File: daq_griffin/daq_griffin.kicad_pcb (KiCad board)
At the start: 4 copper layers, 120 x 120 mm, 223 parts, among them J1 SENSOR, J10 SENSOR, J11 SENSOR, J12 SENSOR, J13 SENSOR, J14 SENSOR, J15 SENSOR, J16 SENSOR, J17 SENSOR, J18 SENSOR, J19 SENSOR, J2 SENSOR, J20 SENSOR, J21 SENSOR, J22 SENSOR, J23 SENSOR, J24 SENSOR, J25 POWER_12V, J26 I2C Header, J27 CAN Header, J28 POWER_24V, J29 POWER_24V, J3 SENSOR, J30 POWER_24V, J31 POWER_24V, J32 POWER_24V, J33 POWER_24V, J34 POWER_24V, J35 POWER_24V, J36 POWER_24V, J37 Conn_01x04_Socket, J38 Conn_01x04_Socket, J39 Conn_01x04_Socket, J4 SENSOR, J40 Conn_01x04_Socket, J41 Conn_01x04_Socket, J42 Conn_01x04_Socket, J43 UART Header, J44 UART Header, J45 Conn_01x03_Socket, J46 Conn_01x03_Socket, J5 SENSOR, J6 SENSOR, J7 SENSOR, J8 SENSOR, J9 SENSOR, U13 ADS8866, U14 ADS8866, U15 ADS8866, U16 ADS8866, U17 ADS8866, U18 ADS8866, U19 ADS8866, U20 ADS8866, U21 ADS8866, U22 ADS8866, U23 ADS8866, U24 ADS8866, U25 TPS54302, U26 Teensy4.1, U29 REF6050xDGK, U30 TLV70933, U55 TCAN3414

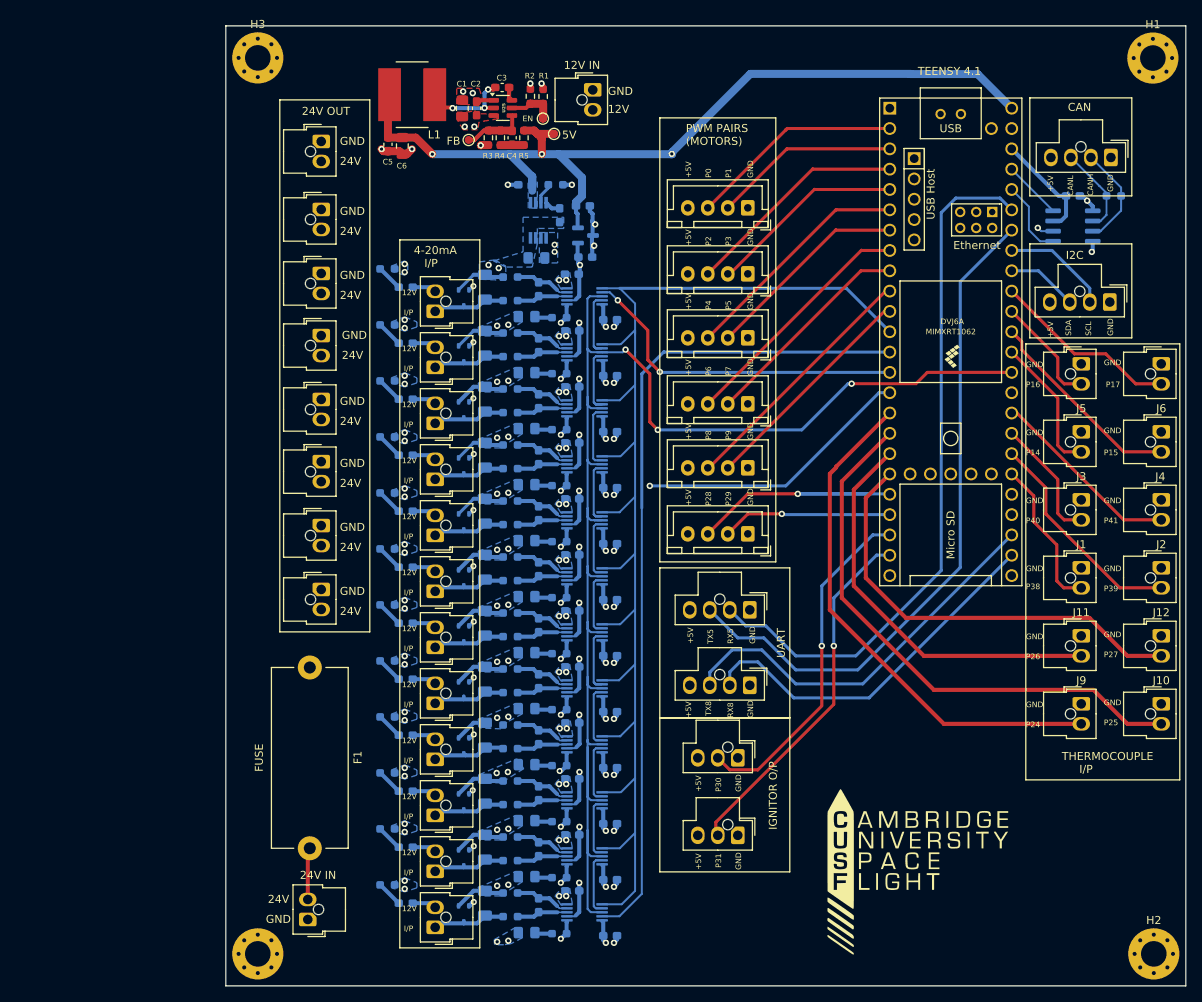
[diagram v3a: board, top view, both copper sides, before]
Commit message: Final touches to silkscreen and hole clearance, names added
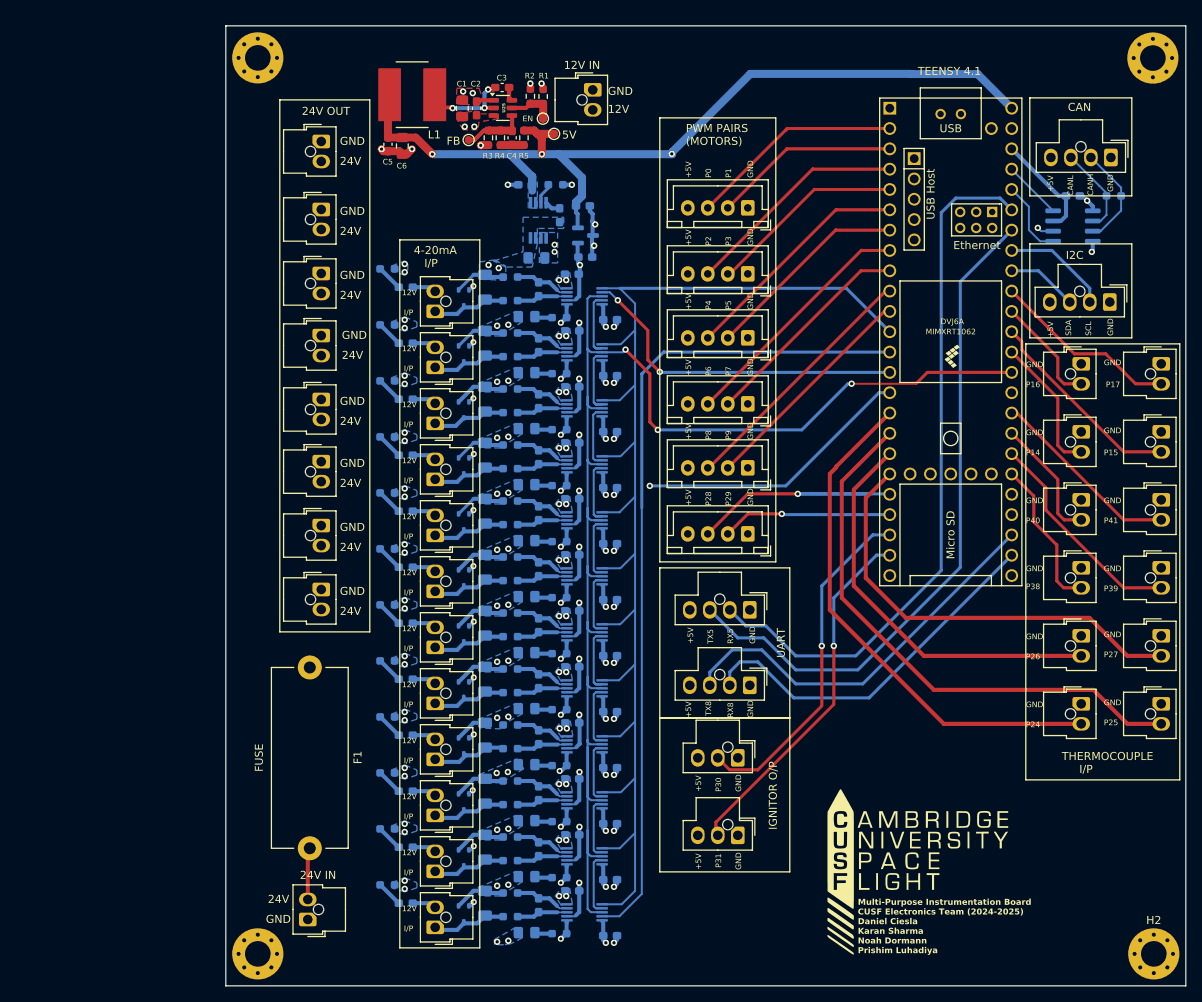
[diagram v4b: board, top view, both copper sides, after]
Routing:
- net /ADC_Chain2/ADC9/SENSOR.IN: track 8.93 -> 9.61 mm
- net /ADC_Chain2/ADC7/SENSOR.IN: track 8.93 -> 9.61 mm
- net /ADC_Chain2/ADC5/SENSOR.IN: track 9.00 -> 9.68 mm
- net /ADC_Chain2/ADC3/SENSOR.IN: track 8.93 -> 9.61 mm
- net /ADC_Chain2/ADC2/SENSOR.IN: track 8.93 -> 9.61 mm
- net /ADC_Chain2/ADC8/SENSOR.IN: track 8.93 -> 9.61 mm
- net /ADC_Chain2/ADC6/SENSOR.IN: track 8.93 -> 9.61 mm
- net /ADC_Chain2/ADC4/SENSOR.IN: track 9.08 -> 9.76 mm
- net /ADC_Chain2/ADC12/SENSOR.IN: track 8.93 -> 9.61 mm
- net /ADC_Chain2/ADC11/SENSOR.IN: track 8.93 -> 9.61 mm
- net /ADC_Chain2/ADC10/SENSOR.IN: track 8.75 -> 9.43 mm
- net /ADC_Chain2/ADC1/SENSOR.IN: track 8.93 -> 9.61 mm
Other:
- board text added: "Multi-Purpose Instrumentation Board CUSF Electronics Team (2024-2025) Daniel Ciesla Karan Sharma Noah Dormann Prishim Luhadiya"

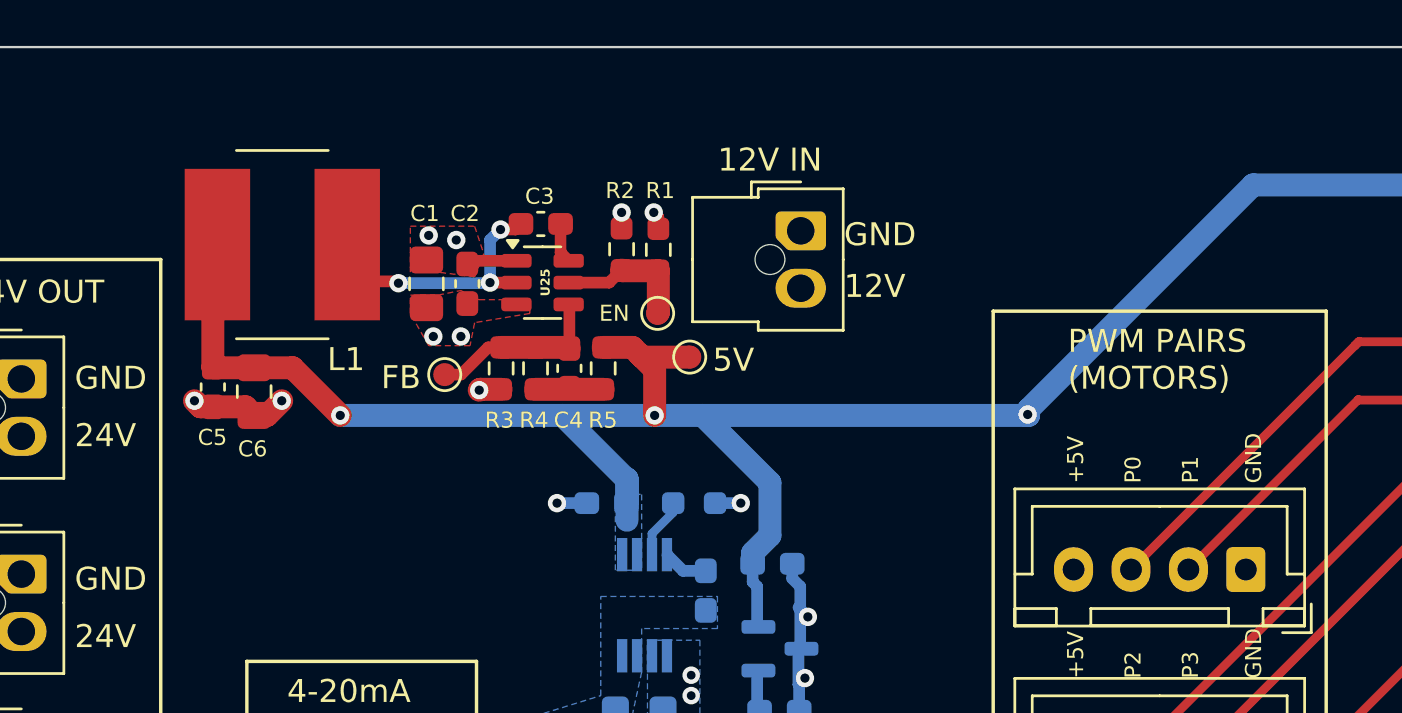
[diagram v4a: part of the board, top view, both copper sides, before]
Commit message: Move 12V - 5V converter circuit to back of board.
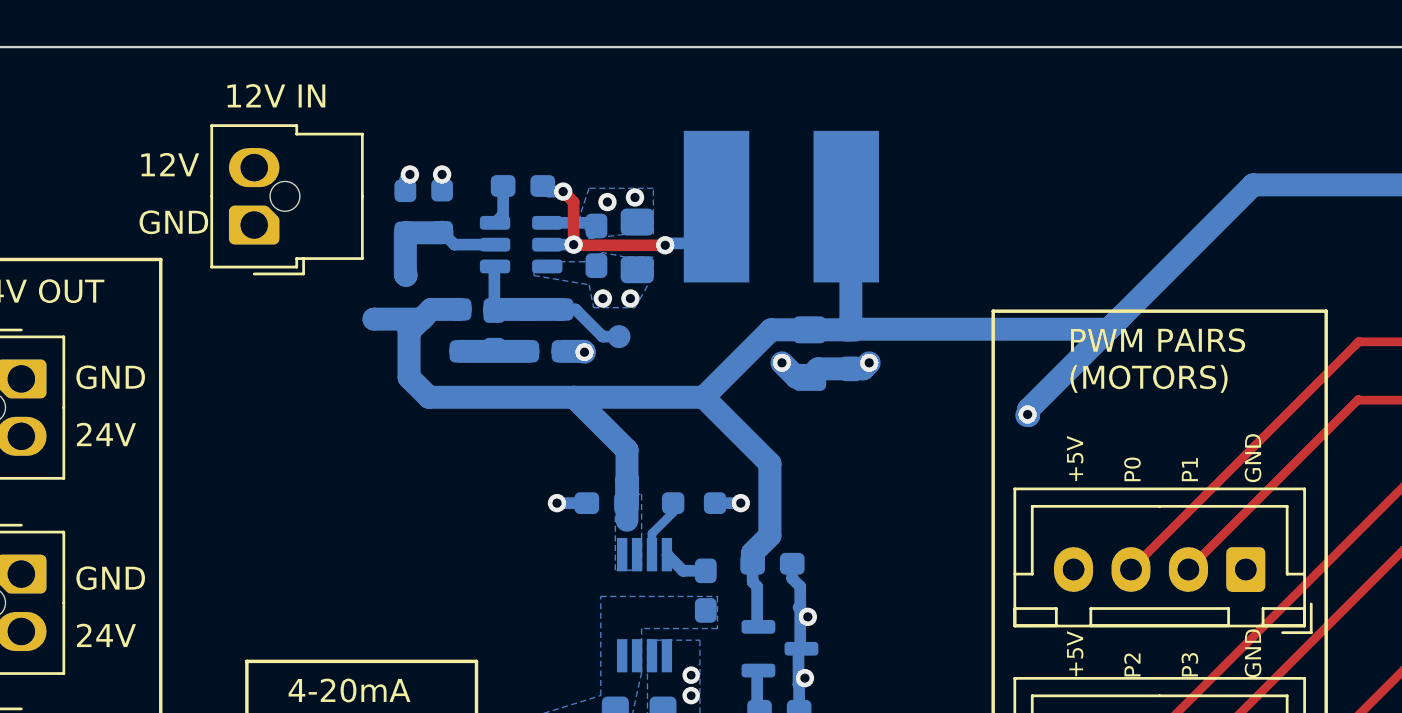
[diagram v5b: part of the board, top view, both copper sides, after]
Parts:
- C1, C2, C3, C4, C5, C6, L1, R1, R2, R3, R4, R5, TP1, TP2, TP3, U25: moved to B.Cu
- moved C5 27.8 mm to (128.1, 71.1)
- moved C6 24.2 mm to (126.3, 71.3)
- moved J25 23.8 mm to (102.1, 65.8), turned to 180 degrees
- moved L1 21.8 mm to (125.0, 64.9), turned to 0 degrees
- moved TP3 13.8 mm to (107.3, 69.8), turned to 180 degrees
- moved R1 11.1 mm to (108.7, 65.2)
- moved TP1 11.1 mm to (108.7, 67.9), turned to 180 degrees
- moved C1 9.33 mm to (118.7, 66.7)
- moved R2 7.99 mm to (110.3, 65.1)
- moved TP2 7.77 mm to (118.0, 70.6), turned to 180 degrees
- moved R5 6.43 mm to (111.1, 70.3)
- moved C2 5.86 mm to (117.0, 66.7)
- moved C4 3.66 mm to (112.5, 70.3)
- moved R3 3.15 mm to (115.5, 70.3)
- moved U25 1.90 mm to (113.7, 66.6), turned to 180 degrees
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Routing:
- net +5V: track 114.7 -> 112.5 mm, vias 3 -> 1
- removed copper zone on F.Cu, net +12V
- removed copper zone on F.Cu, net GND

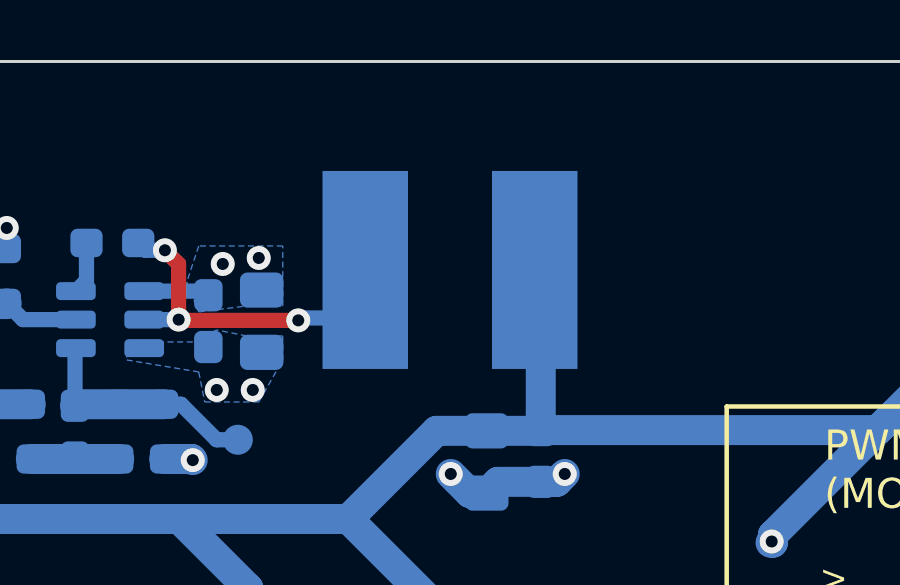
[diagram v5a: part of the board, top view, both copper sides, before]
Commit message: Inductor footprint changed, ADC fuse value now 30mA, ADC 25R resistor now 22R, 0.1-0.47R resistor set to 0.47R
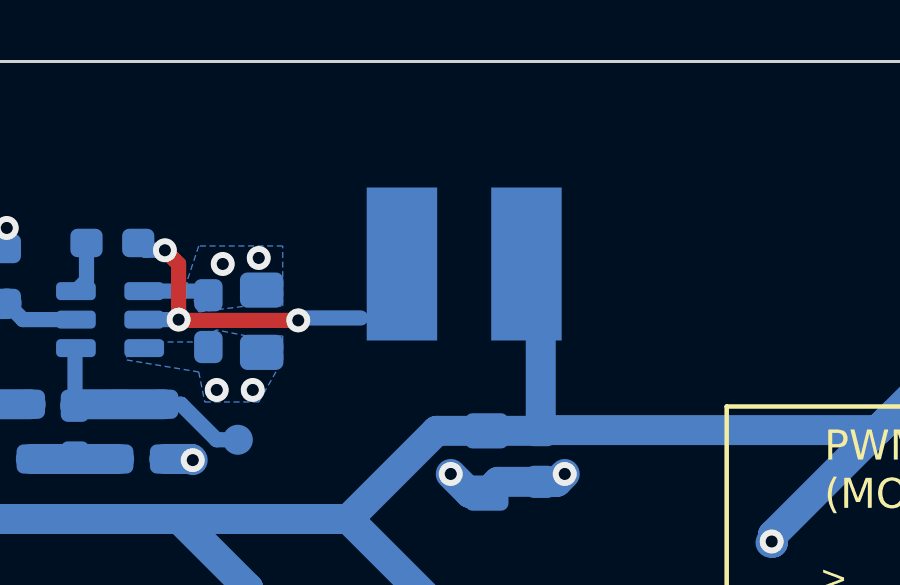
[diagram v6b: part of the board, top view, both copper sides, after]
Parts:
- C110: value 0.1uF -> 100nF
- F13, F14, F15, F16, F17, F18, F19, F20, F21, F22, F23, F24: value 40mA -> 30mA
- L1: footprint Inductor_SMD:L_Bourns_SRN8040TA -> Inductor_SMD:L_Bourns_SRN6045TA
- R130, R131, R132, R133, R134, R135, R136, R137, R138, R139, R140, R141: value 25 -> 22
- moved L1 0.51 mm to (125.5, 64.8)
